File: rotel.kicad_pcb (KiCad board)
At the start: 2 copper layers, 70 x 70 mm, 4 parts

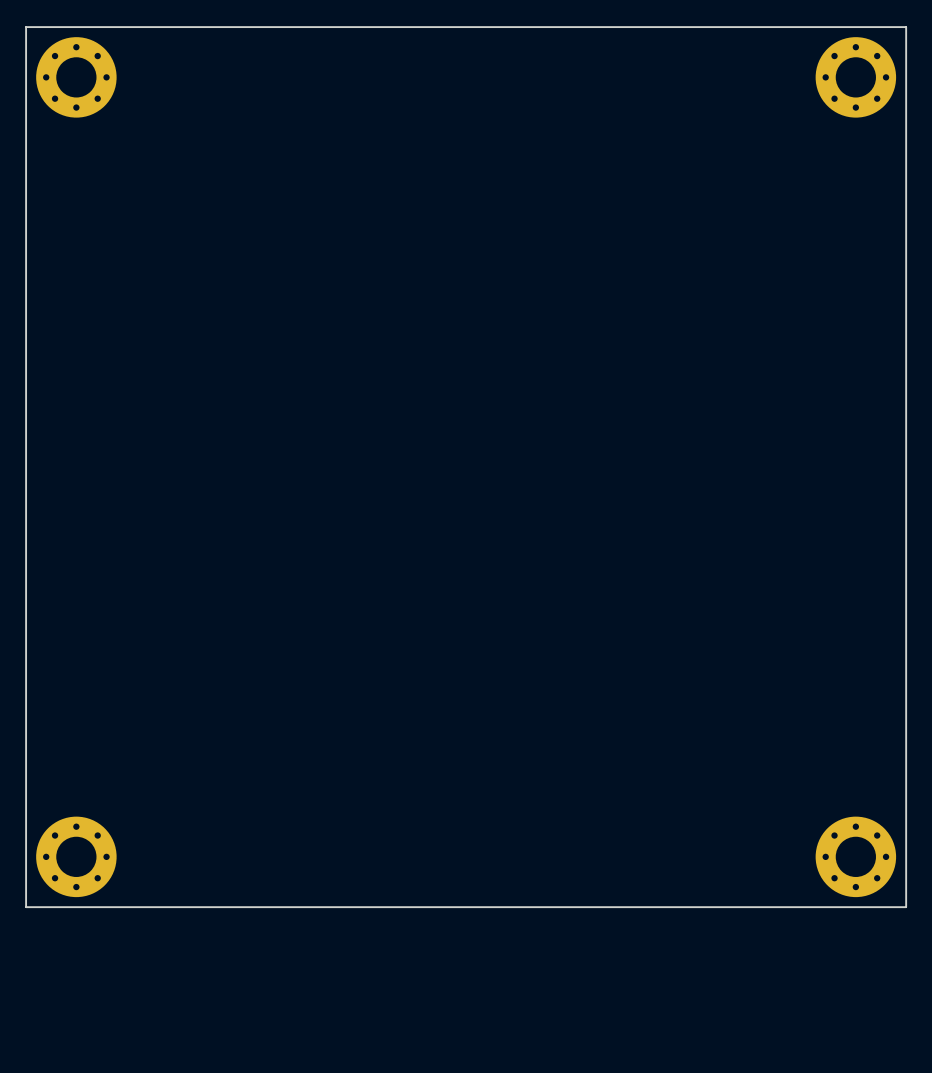
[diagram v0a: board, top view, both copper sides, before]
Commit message: First PCB version. No silkscreen.
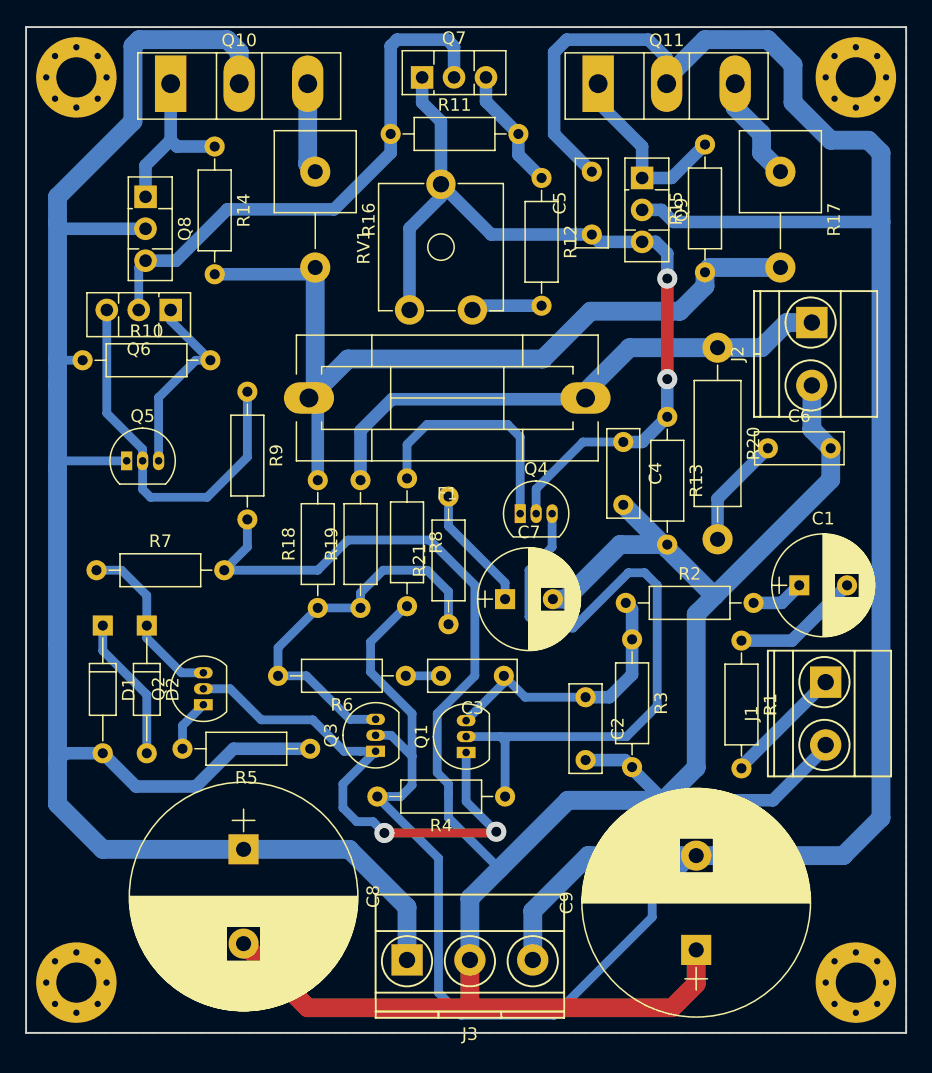
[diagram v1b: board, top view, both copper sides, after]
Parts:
- added C1: 10u_50V, Capacitors_THT:CP_Radial_D8.0mm_P3.80mm, F.Cu at (171.5, 94.4)
- added C2: 100p, Capacitors_THT:C_Rect_L7.0mm_W2.5mm_P5.00mm, F.Cu at (154.5, 103.3)
- added C3: 220p, Capacitors_THT:C_Rect_L7.0mm_W2.5mm_P5.00mm, F.Cu at (148.0, 101.6)
- added C4: 330p, Capacitors_THT:C_Rect_L7.0mm_W2.5mm_P5.00mm, F.Cu at (157.5, 83.0)
- added C5: 150p, Capacitors_THT:C_Rect_L7.0mm_W2.5mm_P5.00mm, F.Cu at (155.0, 66.5)
- added C6: 100n, Capacitors_THT:C_Rect_L7.0mm_W2.5mm_P5.00mm, F.Cu at (169.0, 83.5)
- added C7: 100u_6.3V, Capacitors_THT:CP_Radial_D8.0mm_P3.80mm, F.Cu at (148.1, 95.5)
- added C8: 1000u_63V, Capacitors_THT:CP_Radial_D18.0mm_P7.50mm, F.Cu at (127.3, 115.4)
- added C9: 1000u_63V, Capacitors_THT:CP_Radial_D18.0mm_P7.50mm, F.Cu at (163.3, 123.4)
- added D1: 1N4148, Diodes_THT:D_DO-35_SOD27_P10.16mm_Horizontal, F.Cu at (116.1, 97.6)
- added D2: 1N4148, Diodes_THT:D_DO-35_SOD27_P10.16mm_Horizontal, F.Cu at (119.6, 97.6)
- added F1: T4A, Fuse_Holders_and_Fuses:Fuseholder5x20_horiz_SemiClosed_Casing10x25mm, F.Cu at (154.5, 79.5)
- added J1: In, TerminalBlock_Phoenix:TerminalBlock_Phoenix_MKDS1.5-2pol, F.Cu at (173.6, 102.1)
- added J2: Out, TerminalBlock_Phoenix:TerminalBlock_Phoenix_MKDS1.5-2pol, F.Cu at (172.5, 73.5)
- added J3: Power, TerminalBlock_Phoenix:TerminalBlock_Phoenix_MKDS1.5-3pol, F.Cu at (140.3, 124.2)
- added Q1: 2SA1016K, TO_SOT_Packages_THT:TO-92_Inline_Narrow_Oval, F.Cu at (145.0, 107.7)
- added Q10: 2SD1047, TO_SOT_Packages_THT:TO-247_TO-3P_Vertical, F.Cu at (121.5, 54.5)
- added Q11: 2SB817, TO_SOT_Packages_THT:TO-247_TO-3P_Vertical, F.Cu at (155.5, 54.5)
- added Q2: 2SA1016K, TO_SOT_Packages_THT:TO-92_Inline_Narrow_Oval, F.Cu at (124.1, 103.9)
- added Q3: 2SA1016K, TO_SOT_Packages_THT:TO-92_Inline_Narrow_Oval, F.Cu at (137.8, 107.6)
- added Q4: 2SC1941, TO_SOT_Packages_THT:TO-92_Inline_Narrow_Oval, F.Cu at (149.3, 88.7)
- added Q5: 2SA1016K, TO_SOT_Packages_THT:TO-92_Inline_Narrow_Oval, F.Cu at (118.0, 84.5)
- added Q6: 2SB631K, TO_SOT_Packages_THT:TO-126_Vertical, F.Cu at (121.5, 72.5)
- added Q7: 2SD600K, TO_SOT_Packages_THT:TO-126_Vertical, F.Cu at (141.5, 54.0)
- added Q8: 2SD600K, TO_SOT_Packages_THT:TO-126_Vertical, F.Cu at (119.5, 63.5)
- added Q9: 2SB631K, TO_SOT_Packages_THT:TO-126_Vertical, F.Cu at (159.0, 62.0)
- added R1: 470, Resistors_THT:R_Axial_DIN0207_L6.3mm_D2.5mm_P10.16mm_Horizontal, F.Cu at (166.9, 98.8)
- added R10: 100, Resistors_THT:R_Axial_DIN0207_L6.3mm_D2.5mm_P10.16mm_Horizontal, F.Cu at (114.5, 76.5)
- added R11: 6k8, Resistors_THT:R_Axial_DIN0207_L6.3mm_D2.5mm_P10.16mm_Horizontal, F.Cu at (139.0, 58.5)
- added R12: 2k2, Resistors_THT:R_Axial_DIN0207_L6.3mm_D2.5mm_P10.16mm_Horizontal, F.Cu at (151.0, 62.0)
- added R13: 33k, Resistors_THT:R_Axial_DIN0207_L6.3mm_D2.5mm_P10.16mm_Horizontal, F.Cu at (161.0, 81.0)
- added R14: 220, Resistors_THT:R_Axial_DIN0207_L6.3mm_D2.5mm_P10.16mm_Horizontal, F.Cu at (125.0, 59.5)
- added R15: 220, Resistors_THT:R_Axial_DIN0207_L6.3mm_D2.5mm_P10.16mm_Horizontal, F.Cu at (164.0, 69.5)
- added R16: 0R22, Resistors_THT:R_Axial_Power_L20.0mm_W6.4mm_P7.62mm_Vertical, F.Cu at (133.0, 61.5)
- added R17: 0R22, Resistors_THT:R_Axial_Power_L20.0mm_W6.4mm_P7.62mm_Vertical, F.Cu at (170.0, 61.5)
- added R18: 33k, Resistors_THT:R_Axial_DIN0207_L6.3mm_D2.5mm_P10.16mm_Horizontal, F.Cu at (133.2, 96.2)
- added R19: 12k, Resistors_THT:R_Axial_DIN0207_L6.3mm_D2.5mm_P10.16mm_Horizontal, F.Cu at (136.6, 96.2)
- added R2: 560, Resistors_THT:R_Axial_DIN0207_L6.3mm_D2.5mm_P10.16mm_Horizontal, F.Cu at (157.7, 95.8)
- added R20: 10 _1W, Resistors_THT:R_Axial_DIN0411_L9.9mm_D3.6mm_P15.24mm_Horizontal, F.Cu at (165.0, 75.5)
- added R21: 470, Resistors_THT:R_Axial_DIN0207_L6.3mm_D2.5mm_P10.16mm_Horizontal, F.Cu at (143.6, 97.5)
- added R3: 47k, Resistors_THT:R_Axial_DIN0207_L6.3mm_D2.5mm_P10.16mm_Horizontal, F.Cu at (158.2, 98.7)
- added R4: 1k5, Resistors_THT:R_Axial_DIN0207_L6.3mm_D2.5mm_P10.16mm_Horizontal, F.Cu at (148.1, 111.2)
- added R5: 470, Resistors_THT:R_Axial_DIN0207_L6.3mm_D2.5mm_P10.16mm_Horizontal, F.Cu at (132.6, 107.4)
- added R6: 330, Resistors_THT:R_Axial_DIN0207_L6.3mm_D2.5mm_P10.16mm_Horizontal, F.Cu at (140.2, 101.6)
- added R7: 6k8, Resistors_THT:R_Axial_DIN0207_L6.3mm_D2.5mm_P10.16mm_Horizontal, F.Cu at (115.6, 93.2)
- added R8: 47, Resistors_THT:R_Axial_DIN0207_L6.3mm_D2.5mm_P10.16mm_Horizontal, F.Cu at (140.3, 85.9)
- added R9: 10k, Resistors_THT:R_Axial_DIN0207_L6.3mm_D2.5mm_P10.16mm_Horizontal, F.Cu at (127.6, 79.0)
- added RV1: 2k2, Potentiometers:Potentiometer_Trimmer_ACP_CA9v_Horizontal_Px10.0mm_Py5.0mm, F.Cu at (145.5, 72.5)
- moved REF** 10.0 mm to (176.0, 126.0)
- moved REF** 10.0 mm to (114.0, 126.0)
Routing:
- net Net-(C5-Pad2): track 0.00 -> 223.2 mm
- net GND: track 0.00 -> 206.0 mm
- net Net-(C8-Pad1): track 0.00 -> 148.4 mm
- net Net-(F1-Pad2): track 0.00 -> 68.8 mm
- net Net-(C4-Pad1): track 0.00 -> 68.2 mm, vias 0 -> 2
- net Net-(Q1-Pad2): track 0.00 -> 52.5 mm
- net Net-(F1-Pad1): track 0.00 -> 43.7 mm
- net Net-(Q6-Pad2): track 0.00 -> 43.7 mm
- net Net-(Q1-Pad1): track 0.00 -> 41.9 mm, vias 0 -> 2
- net Net-(Q3-Pad3): track 0.00 -> 31.6 mm
- net Net-(Q5-Pad2): track 0.00 -> 30.6 mm
- net Net-(C2-Pad1): track 0.00 -> 22.4 mm
- net Net-(Q4-Pad1): track 0.00 -> 19.5 mm
- net Net-(Q5-Pad3): track 0.00 -> 15.7 mm
- net Net-(Q11-Pad1): track 0.00 -> 15.1 mm
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- added copper zone on F.Cu, net GND
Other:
- board size 70 x 70 mm -> 70 x 80 mm
